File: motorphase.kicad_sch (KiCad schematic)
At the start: 13 parts, among them J4 Motor Connection, Q1 CSD88584Q5DCT

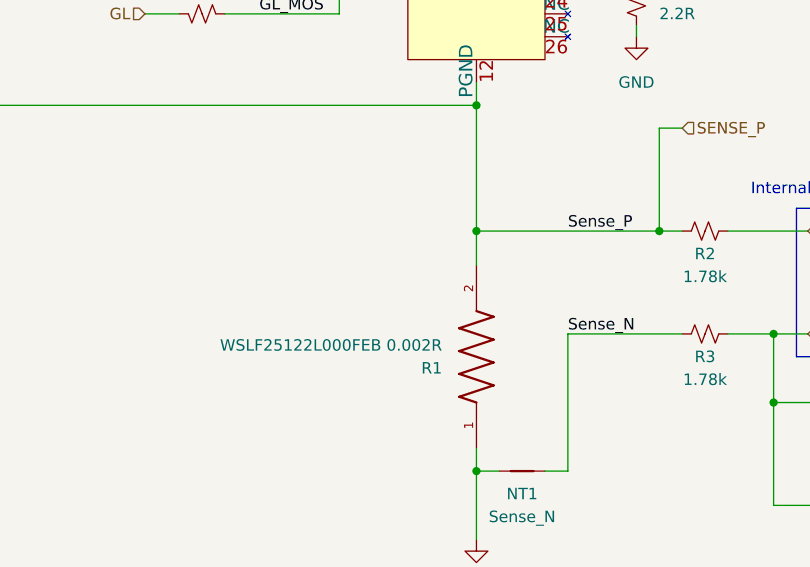
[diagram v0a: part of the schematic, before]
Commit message: added rs485 and placed ma702
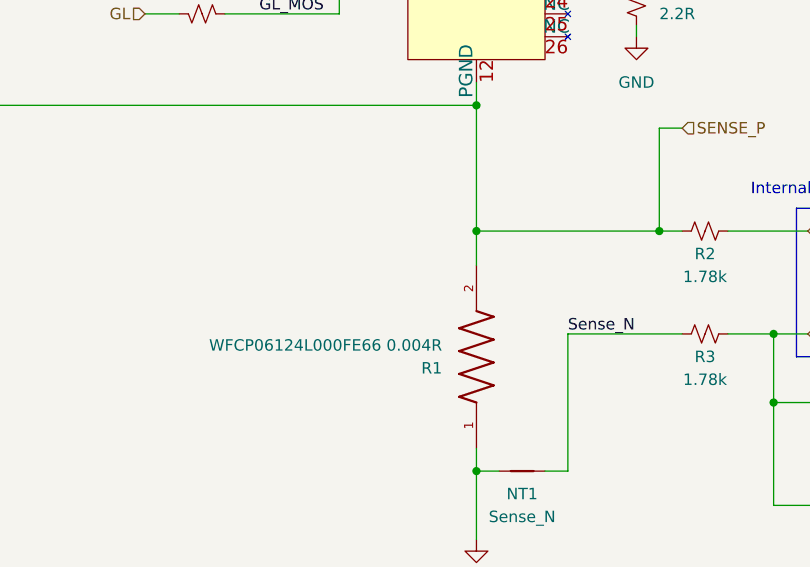
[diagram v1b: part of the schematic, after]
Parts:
- R1: value WSLF25122L000FEB 0.002R -> WFCP06124L000FE66 0.004R; footprint RESC2550X76N -> Resistor_SMD:R_Shunt_2512_6332Metric; symbol O32controller:WSLF25122L000FEB -> O32controller:WFCP06124L000FE66
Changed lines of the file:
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@@
-    (effects (font (size 1.27 1.27)) (justify left bottom))
-  )
-  (label "Sense_P" (at 138.43 120.65 0)
     (effects (font (size 1.27 1.27)) (justify left bottom))
   )
@@
     (pin "3")
   )
-  (symbol (lib_id "O32controller:WSLF25122L000FEB") (at 128.27 134.62 90) (unit 1)
+  (symbol (lib_id "O32controller:WFCP06124L000FE66") (at 128.27 134.62 90) (unit 1)
     (in_bom yes) (on_board yes)
     (property "Reference" "R1" (id 0) (at 124.46 135.8901 90)
       (effects (font (size 1.27 1.27)) (justify left))
     )
-    (property "Value" "WSLF25122L000FEB 0.002R" (id 1) (at 124.46 133.3501 90)
-      (effects (font (size 1.27 1.27)) (justify left))
-    )
-    (property "Footprint" "RESC2550X76N" (id 2) (at 128.27 134.62 0)
+    (property "Value" "WFCP06124L000FE66 0.004R" (id 1) (at 124.46 133.3501 90)
+      (effects (font (size 1.27 1.27)) (justify left))
+    )
+    (property "Footprint" "Resistor_SMD:R_Shunt_2512_6332Metric" (id 2) (at 128.27 134.62 0)
       (effects (font (size 1.27 1.27)) (justify bottom) hide)
     )
-    (property "Datasheet" "" (id 3) (at 128.27 134.62 0)
-      (effects (font (size 1.27 1.27)) hide)
-    )
+    (property "Datasheet" "https://www.vishay.com/docs/30417/wfcp.pdf" (id 3) (at 128.27 134.62 0)
+      (effects (font (size 1.27 1.27)) hide)
+    )

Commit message: ahh my resistor schematic is old:
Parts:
- added R? (x2): 27.4k, Resistor_SMD:R_0402_1005Metric, symbol Device:R_Small_US
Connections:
- net GND: now also R?.1
- net OP_P: now also R?.1, R?.2
- new net +3.3V: R?.2
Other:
- note added: "Special resistor 1/8W 0402"
- note added: "pls fix resistor"
- moved on the sheet: C18, R2, R3, R4

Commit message: woohoo everything connected, no drc err
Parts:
- C13: MP (none) -> GRM155R72A472KA01D
- Q1: MP (none) -> CSD88584Q5DCT
- R1: value WFCP06124L000FE66 0.004R -> WSLF25122L000FEB 0.002R; MP (none) -> WSLF25122L000FEB 0.002R
- gave numbers to parts that had none: 2
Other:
- note added: "1/4W 0402"
- note removed: "Special resistor 1/8W 0402"
- note removed: "pls fix resistor"
- moved on the sheet: C12, C13, C18, J4, NT1, Q1, R1, R13, R15, R2, R23, R3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

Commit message: finish, generate gerbers
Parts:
- C12: MP (none) -> CL05B103KB5NNNC
- C18: MP (none) -> CC0402MRX7R9BB102
- R13, R15: MP (none) -> RCS040210R0FKED
- R2, R3: MP (none) -> RC0402FR-071K78L
- R23: MP (none) -> SG73P1EWTTP2R20F
- R30, R31: MP (none) -> RC0402FR-0727K4L
- R4: MP (none) -> RC0402FR-0713K7L
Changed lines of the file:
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@@
       (effects (font (size 1.27 1.27)) hide)
     )
-    (property "Datasheet" "~" (id 3) (at 146.05 104.14 0)
+    (property "Datasheet" "https://www.yageo.com/upload/media/product/productsearch/datasheet/rchip/PYu-RC_Group_51_RoHS_L_12.pdf" (id 3) (at 146.05 104.14 0)
+      (effects (font (size 1.27 1.27)) hide)
+    )
+    (property "MP" "RC0402FR-071K78L " (id 4) (at 146.05 104.14 0)
       (effects (font (size 1.27 1.27)) hide)
     )
@@
       (effects (font (size 1.27 1.27)) hide)
     )
-    (property "Datasheet" "~" (id 3) (at 97.79 80.01 0)
+    (property "Datasheet" "https://www.vishay.com/docs/20065/rcse3.pdf" (id 3) (at 97.79 80.01 0)
+      (effects (font (size 1.27 1.27)) hide)
+    )
+    (property "MP" "RCS040210R0FKED " (id 4) (at 97.79 80.01 0)
       (effects (font (size 1.27 1.27)) hide)
     )
@@
     )
     (property "Datasheet" "https://www.digikey.com/en/products/detail/koa-speer-electronics-inc/SG73P1EWTTP2R20F/14316750" (id 3) (at 146.05 78.74 0)
+      (effects (font (size 1.27 1.27)) hide)
+    )
+    (property "MP" "SG73P1EWTTP2R20F " (id 4) (at 146.05 78.74 0)
       (effects (font (size 1.27 1.27)) hide)
     )
@@
       (effects (font (size 1.27 1.27)) hide)
     )
-    (property "Datasheet" "~" (id 3) (at 71.12 69.85 0)
+    (property "Datasheet" "https://media.digikey.com/pdf/Data%20Sheets/Samsung%20PDFs/CL05B103KB5NNN_Spec.pdf" (id 3) (at 71.12 69.85 0)
+      (effects (font (size 1.27 1.27)) hide)
+    )
+    (property "MP" "CL05B103KB5NNNC" (id 4) (at 71.12 69.85 0)
       (effects (font (size 1.27 1.27)) hide)
     )
@@
       (effects (font (size 1.27 1.27)) hide)
     )
-    (property "Datasheet" "~" (id 3) (at 160.02 101.6 0)
+    (property "Datasheet" "https://www.yageo.com/upload/media/product/productsearch/datasheet/rchip/PYu-RC_Group_51_RoHS_L_12.pdf" (id 3) (at 160.02 101.6 0)
+      (effects (font (size 1.27 1.27)) hide)
+    )
+    (property "MP" "RC0402FR-0727K4L " (id 4) (at 160.02 101.6 0)
       (effects (font (size 1.27 1.27)) hide)
     )
@@
       (effects (font (size 1.27 1.27)) hide)
     )
-    (property "Datasheet" "~" (id 3) (at 160.02 106.68 0)
+    (property "Datasheet" "https://www.yageo.com/upload/media/product/productsearch/datasheet/rchip/PYu-RC_Group_51_RoHS_L_12.pdf" (id 3) (at 160.02 106.68 0)
+      (effects (font (size 1.27 1.27)) hide)
+    )
+    (property "MP" "RC0402FR-0727K4L " (id 4) (at 160.02 106.68 0)
       (effects (font (size 1.27 1.27)) hide)
     )
@@
       (effects (font (size 1.27 1.27)) hide)
     )
-    (property "Datasheet" "~" (id 3) (at 181.61 123.19 0)
+    (property "Datasheet" "https://www.yageo.com/upload/media/product/productsearch/datasheet/rchip/PYu-RC_Group_51_RoHS_L_12.pdf" (id 3) (at 181.61 123.19 0)
+      (effects (font (size 1.27 1.27)) hide)
+    )
+    (property "MP" "RC0402FR-0713K7L " (id 4) (at 181.61 123.19 0)
       (effects (font (size 1.27 1.27)) hide)
     )
@@
       (effects (font (size 1.27 1.27)) hide)
     )
-    (property "Datasheet" "~" (id 3) (at 181.61 134.62 0)
+    (property "Datasheet" "https://www.yageo.com/upload/media/product/productsearch/datasheet/mlcc/UPY-GPHC_X7R_6.3V-to-250V_22.pdf" (id 3) (at 181.61 134.62 0)
+      (effects (font (size 1.27 1.27)) hide)
+    )
+    (property "MP" "CC0402MRX7R9BB102" (id 4) (at 181.61 134.62 0)
       (effects (font (size 1.27 1.27)) hide)
     )
@@
       (effects (font (size 1.27 1.27)) hide)
     )
-    (property "Datasheet" "~" (id 3) (at 97.79 62.23 0)
+    (property "Datasheet" "https://www.vishay.com/docs/20065/rcse3.pdf" (id 3) (at 97.79 62.23 0)
+      (effects (font (size 1.27 1.27)) hide)
+    )
+    (property "MP" "RCS040210R0FKED " (id 4) (at 97.79 62.23 0)
       (effects (font (size 1.27 1.27)) hide)
     )
@@
       (effects (font (size 1.27 1.27)) hide)
     )
-    (property "Datasheet" "~" (id 3) (at 146.05 115.57 0)
-      (effects (font (size 1.27 1.27)) hide)
-    )
+    (property "Datasheet" "https://www.yageo.com/upload/media/product/productsearch/datasheet/rchip/PYu-RC_Group_51_RoHS_L_12.pdf" (id 3) (at 146.05 115.57 0)
+      (effects (font (size 1.27 1.27)) hide)
+    )
+    (property "MP" "RC0402FR-071K78L " (id 4) (at 146.05 115.57 0)
+      (effects (font (size 1.27 1.27)) hide)
+    )

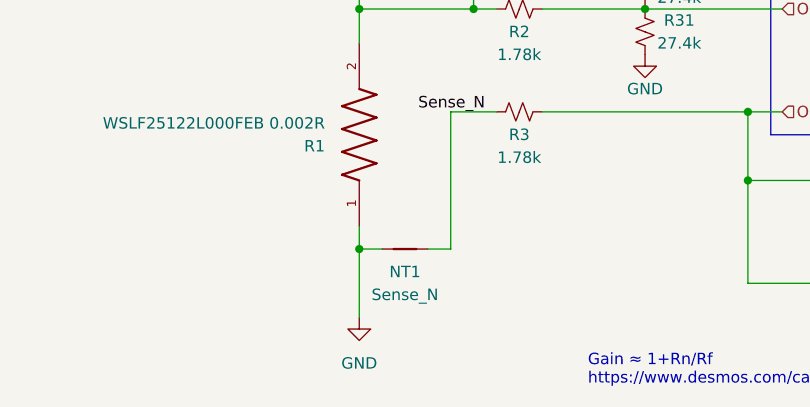
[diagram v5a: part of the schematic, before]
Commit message: clean up v2, fix libraries, netties, fix TVS dir
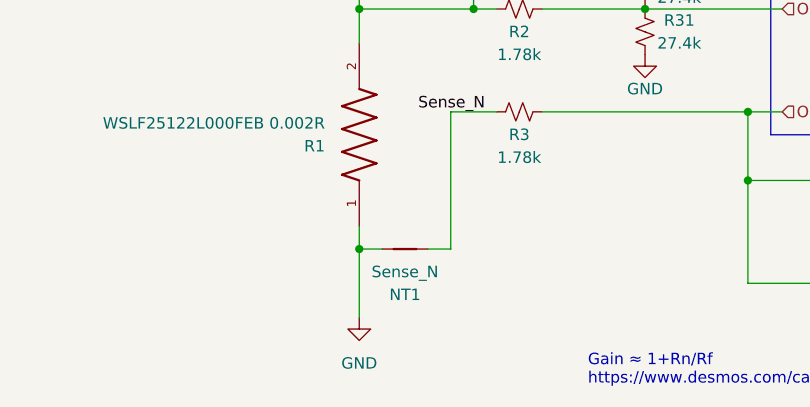
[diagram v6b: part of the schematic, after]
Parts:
- NT1: footprint NetTie:NetTie-small -> O32controller:NetTie-2_SMD_Pad0.25mm; now left out of the parts list
- R1: footprint Resistor_SMD:R_Shunt_2512_6332Metric -> O32controller:R_Shunt_2512_6332Metric

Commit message: remove motor conn from ibom, reannotate tvs diode
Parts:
- J4: now left out of the parts list
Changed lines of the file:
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@@
   )
   (symbol (lib_id "Connector_Generic:Conn_01x01") (at 170.18 67.31 0) (unit 1)
-    (in_bom yes) (on_board yes) (dnp no) (fields_autoplaced)
+    (in_bom no) (on_board yes) (dnp no) (fields_autoplaced)
     (property "Reference" "J4" (at 172.72 66.0399 0)
       (effects (font (size 1.27 1.27)) (justify left))
